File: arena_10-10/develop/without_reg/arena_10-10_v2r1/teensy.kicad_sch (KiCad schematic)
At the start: 41 parts, among them J1 Cetus RJ45 Magjack, J2 Conn_01x02, J3 Conn_Coaxial, J30 Conn_01x02, J4 Conn_Coaxial, U1 Teensy4.1, U2 SN74LVC1T45DBV, U3 SN74LVC1T45DBV

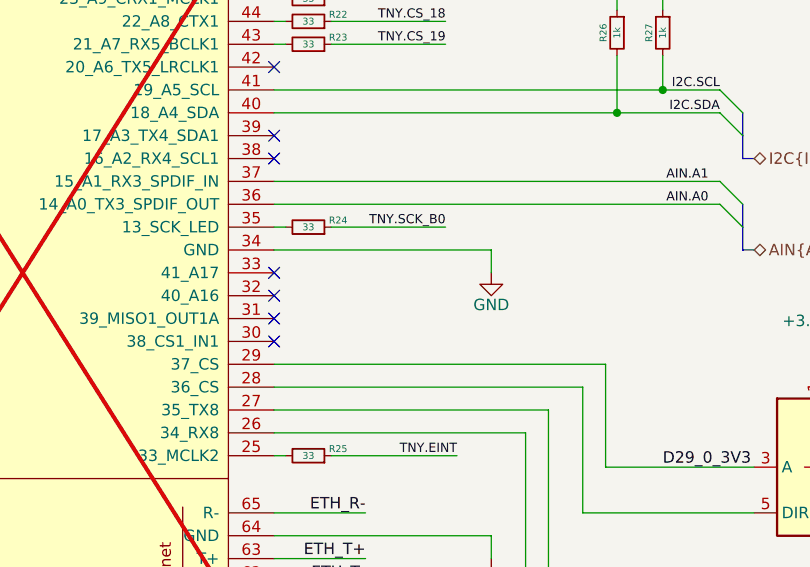
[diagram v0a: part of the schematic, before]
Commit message: Made modifications to efuse circuit and added some notes.
Modified efuse so that switch is now is EN/UVLO leg. Added 1k
resistors for extra wetting current - so we can use any old switch.
Upped capacitors size to help with switch debounce. Added 1k resistor
between TVL6700 and EN/UVLO. This is to deal with current when OUTB
discharges the larger EN capacitor.
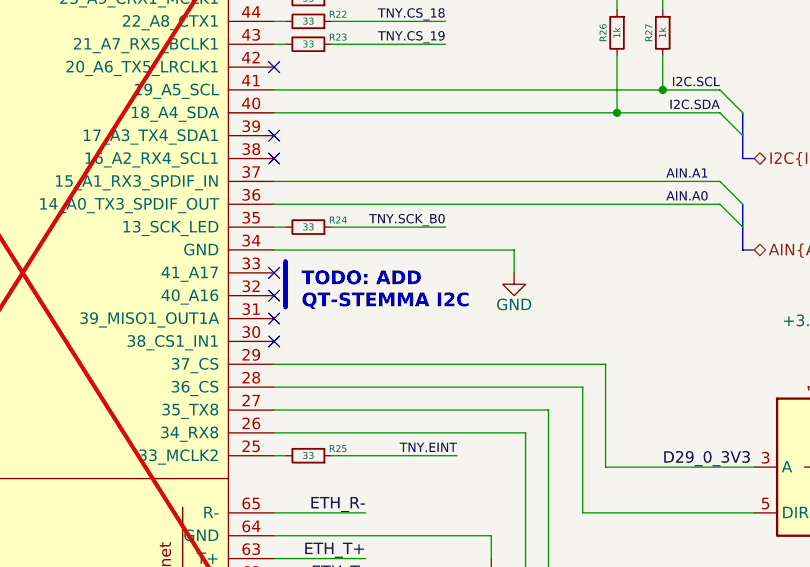
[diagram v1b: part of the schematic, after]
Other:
- note added: "TODO: ADD QT-STEMMA I2C"
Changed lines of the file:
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@@
 		)
 	)
+	(text "TODO: ADD \nQT-STEMMA I2C"
+		(exclude_from_sim no)
+		(at 108.458 78.232 0)
+		(effects
+			(font
+				(size 1.524 1.524)
+				(thickness 0.254)
+				(bold yes)
+			)
+			(justify left)
+		)
+	)
 	(text "SPI BUS B1"
 		(exclude_from_sim no)
@@
 	(wire
 		(pts
-			(xy 105.41 73.66) (xy 129.54 73.66)
+			(xy 105.41 73.66) (xy 132.08 73.66)
 		)
 		(stroke
@@
 	(wire
 		(pts
-			(xy 129.54 73.66) (xy 129.54 76.2)
+			(xy 132.08 73.66) (xy 132.08 76.2)
 		)
 		(stroke
@@
 		)
 	)
+	(polyline
+		(pts
+			(xy 106.68 74.93) (xy 106.68 80.01)
+		)
+		(stroke
+			(width 0.508)
+			(type solid)
+		)
+	)
 	(wire
 		(pts
@@
 		(lib_name "GND_1")
 		(lib_id "power:GND")
-		(at 129.54 76.2 0)
+		(at 132.08 76.2 0)
 		(unit 1)
 		(body_style 1)
@@
 		(dnp no)
 		(property "Reference" "#PWR05"
-			(at 129.54 82.55 0)
+			(at 132.08 82.55 0)
 			(hide yes)
 			(show_name no)
@@
 		)
 		(property "Value" "GND"
-			(at 129.54 79.756 0)
+			(at 132.08 79.756 0)
 			(show_name no)
 			(do_not_autoplace no)
@@
 		)
 		(property "Footprint" ""
-			(at 129.54 76.2 0)
+			(at 132.08 76.2 0)
 			(hide yes)
 			(show_name no)
@@
 		)
 		(property "Datasheet" ""
-			(at 129.54 76.2 0)
+			(at 132.08 76.2 0)
 			(hide yes)
 			(show_name no)
@@
 		)
 		(property "Description" "Power symbol creates a global label with name \"GND\" , ground"
-			(at 129.54 76.2 0)
+			(at 132.08 76.2 0)
 			(hide yes)
 			(show_name no)

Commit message: Added clamp to IMON.  Connected PG and IMON to teensy.
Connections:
- net PG: now reaches U1.31 (39_MISO1_OUT1A)
- net IMON: now reaches U1.32 (40_A16)
- no-connect marks 10 -> 8
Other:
- note added: "Power Monitoring Signals"
- moved on the sheet: C140, C141, C2, C3

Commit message: Added analog island to 10-10 arena with efuse.
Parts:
- added J31: Conn_01x04, Package_DFN_QFN:WDFN-10-1EP_3x3mm_P0.5mm_EP1.8x2.5mm, symbol Connector_Generic:Conn_01x04
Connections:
- net +3.3V: now also J31.2 (Pin_2)
- net GND: now also J31.1 (Pin_1)
- net SCL1: now reaches U1.38 (16_A2_RX4_SCL1)
- net SCL1: now also J31.4 (Pin_4)
- net SDA1: now reaches U1.39 (17_A3_TX4_SDA1)
- net SDA1: now also J31.3 (Pin_3)
- no-connect marks 8 -> 6
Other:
- note removed: "TODO: ADD QT-STEMMA I2C"
- moved on the sheet: C1, C140, C141, C2, C3, J1
